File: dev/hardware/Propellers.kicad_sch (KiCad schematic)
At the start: 6 parts, among them SW1 RESET SW, U1 P8X32A-D40, Y1 6.5MHz

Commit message: Continued developing JCAP schematic
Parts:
- added C1, C2: 0.1u, Capacitor_THT:C_Radial_D4.0mm_H7.0mm_P1.50mm, symbol Device:C
- added R1: 1K, Resistor_THT:R_Axial_DIN0207_L6.3mm_D2.5mm_P10.16mm_Horizontal, symbol Device:R
- added SW1: RESET SW, symbol Switch:SW_MEC_5E
- added U1: P8X32A-D40, Package_DIP:DIP-40_W15.24mm_Socket, symbol MCU_Parallax:P8X32A-D40
- added Y1: 6.5MHz, Crystal:Crystal_HC49-U_Vertical, symbol Device:Crystal
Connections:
- net +3.3V: now also C1.2, C2.1
- net GND: now also R1.1, U1.10 (~{BOE}), U1.29 (VSS), U1.9 (VSS)
- net INPUTS_CLK: now reaches U1.34 (P25)
- net INPUTS_PL_N: now reaches U1.35 (P26)
- net INPUTS: now reaches U1.36 (P27)
- net SCL_CPU: now reaches U1.37 (P28)
- net SDA_CPU: now reaches U1.38 (P29)
- net SER_TX_CPU: now reaches U1.39 (P30)
- net SER_RX_CPU: now reaches U1.40 (P31)
- net SER_RES_N_CPU: now reaches SW1.3 (K)
- new net: C1.1, U1.12 (VDD)
- new net: U1.31 (XO), Y1.1
- new net: U1.30 (XI), Y1.2
- new net: SW1.4 (A), U1.11 (~{RES})
- new net: C2.2, U1.32 (VDD)
- new net: R1.2, SW1.1
- new net BLUE0: U1.27 (P22)
- new net BLUE1: U1.28 (P23)
- new net GREEN0: U1.24 (P19)
- new net GREEN1: U1.25 (P20)
- new net GREEN2: U1.26 (P21)
- new net H_SYNC: U1.34 (P25)
- new net RED0: U1.21 (P16)
- new net RED1: U1.22 (P17)
- new net RED2: U1.23 (P18)
- new net SCL_GPU: U1.37 (P28)
- new net SDA_GPU: U1.38 (P29)
- new net SER_RES_N_GPU: SW1.3 (K)
- new net SER_RX_GPU: U1.40 (P31)
- new net SER_TX_GPU: U1.39 (P30)
- new net V_SYNC: U1.33 (P24)
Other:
- moved on the sheet: C1, C2, R1, SW1, U1, Y1

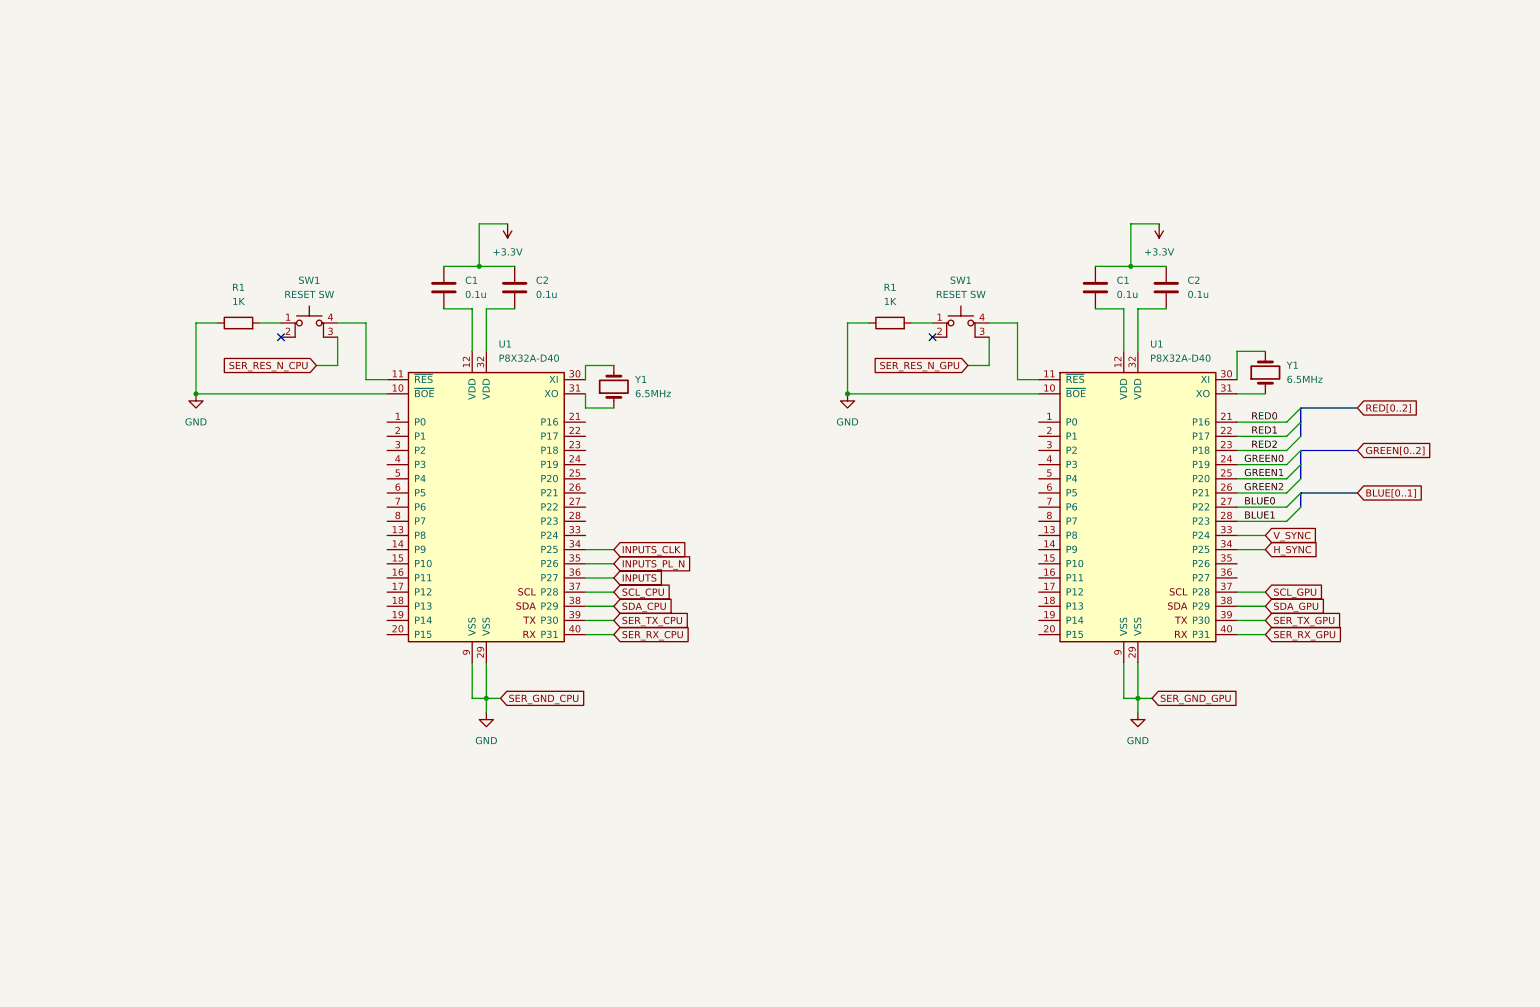
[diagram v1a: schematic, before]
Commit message: Finalized initial schematic
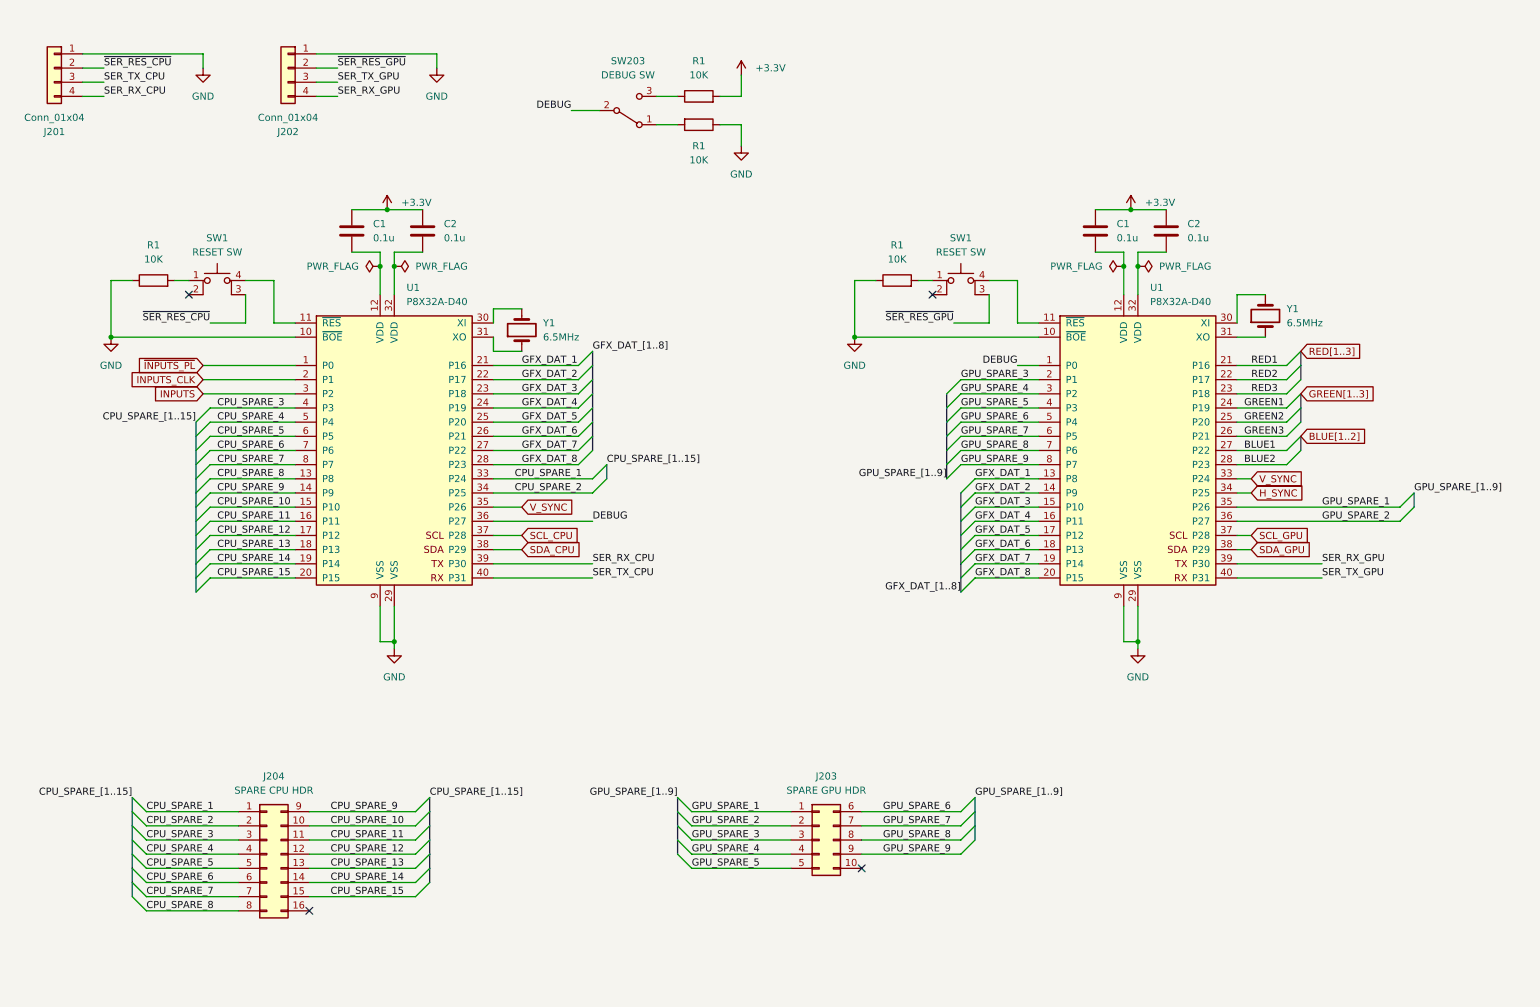
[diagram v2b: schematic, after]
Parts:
- removed R1 (x2): 1K, Resistor_THT:R_Axial_DIN0207_L6.3mm_D2.5mm_P10.16mm_Horizontal, symbol Device:R
- removed SW1 (x2): RESET SW, symbol Switch:SW_MEC_5E
- added J201, J202: Conn_01x04, Connector_PinHeader_2.54mm:PinHeader_1x04_P2.54mm_Horizontal, symbol Connector_Generic:Conn_01x04
- added J203: SPARE GPU HDR, Connector_PinHeader_2.54mm:PinHeader_2x05_P2.54mm_Vertical, symbol Connector_Generic:Conn_02x05_Top_Bottom
- added J204: SPARE CPU HDR, Connector_PinHeader_2.54mm:PinHeader_2x08_P2.54mm_Vertical, symbol Connector_Generic:Conn_02x08_Top_Bottom
- added R1 (x4): 10K, Resistor_THT:R_Axial_DIN0207_L6.3mm_D2.5mm_P10.16mm_Horizontal, symbol Device:R
- added SW1 (x2): RESET SW, Button_Switch_THT:SW_PUSH_6mm_H5mm, symbol Switch:SW_MEC_5E
- added SW203: DEBUG SW, Button_Switch_THT:SW_E-Switch_EG1271_SPDT, symbol Switch:SW_SPDT
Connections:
- net BLUE0 is gone; now on net BLUE1: U1.27 (P22)
- net GREEN0 is gone; now on net GREEN1: U1.24 (P19)
- net INPUTS_PL_N is gone; now on net V_SYNC: U1.35 (P26)
- net RED0 is gone; now on net RED1: U1.21 (P16)
- net +3.3V: now also R1.2
- net BLUE1: no longer U1.28 (P23)
- net GND: now also J201.1 (Pin_1), J202.1 (Pin_1), R1.1, R1.1, R1.1
- net GREEN1: no longer U1.25 (P20)
- net GREEN2: now also U1.25 (P20); no longer U1.26 (P21)
- net INPUTS: now also U1.3 (P2); no longer U1.36 (P27)
- net INPUTS_CLK: now also U1.2 (P1); no longer U1.34 (P25)
- net RED1: no longer U1.22 (P17)
- net RED2: now also U1.22 (P17); no longer U1.23 (P18)
- net SER_RX_CPU: now also U1.39 (P30), J201.4 (Pin_4); no longer U1.40 (P31)
- net SER_RX_GPU: now also U1.39 (P30), J202.4 (Pin_4); no longer U1.40 (P31)
- net SER_TX_CPU: now also U1.40 (P31), J201.3 (Pin_3); no longer U1.39 (P30)
- net SER_TX_GPU: now also U1.40 (P31), J202.3 (Pin_3); no longer U1.39 (P30)
- net DEBUG: now reaches U1.1 (P0)
- net DEBUG: now also U1.36 (P27), SW203.2 (B)
- net at U1.11 (~{RES}): now also SW1.4 (A) (x2)
- net GFX_DAT_1: now reaches U1.13 (P8)
- net GFX_DAT_1: now also U1.21 (P16)
- net GFX_DAT_2: now reaches U1.14 (P9)
- net GFX_DAT_2: now also U1.22 (P17)
- net GFX_DAT_3: now reaches U1.15 (P10)
- net GFX_DAT_3: now also U1.23 (P18)
- net GFX_DAT_4: now reaches U1.16 (P11)
- net GFX_DAT_4: now also U1.24 (P19)
- net GFX_DAT_5: now reaches U1.17 (P12)
- net GFX_DAT_5: now also U1.25 (P20)
- net GFX_DAT_6: now reaches U1.18 (P13)
- net GFX_DAT_6: now also U1.26 (P21)
- net GFX_DAT_7: now reaches U1.19 (P14)
- net GFX_DAT_7: now also U1.27 (P22)
- net GPU_SPARE_3: now reaches U1.2 (P1)
- net GPU_SPARE_3: now also J203.3 (Pin_3)
- net GFX_DAT_8: now reaches U1.20 (P15)
- net GFX_DAT_8: now also U1.28 (P23)
- net GPU_SPARE_4: now reaches U1.3 (P2)
- net GPU_SPARE_4: now also J203.4 (Pin_4)
- net GPU_SPARE_1: now reaches U1.35 (P26)
- net GPU_SPARE_1: now also J203.1 (Pin_1)
- net GPU_SPARE_2: now reaches U1.36 (P27)
- net GPU_SPARE_2: now also J203.2 (Pin_2)
- net GPU_SPARE_5: now reaches U1.4 (P3)
- net GPU_SPARE_5: now also J203.5 (Pin_5)
- net GPU_SPARE_6: now reaches U1.5 (P4)
- net GPU_SPARE_6: now also J203.6 (Pin_6)
- net GPU_SPARE_7: now reaches U1.6 (P5)
- net GPU_SPARE_7: now also J203.7 (Pin_7)
- net GPU_SPARE_8: now reaches U1.7 (P6)
- net GPU_SPARE_8: now also J203.8 (Pin_8)
- net GPU_SPARE_9: now reaches U1.8 (P7)
- net GPU_SPARE_9: now also J203.9 (Pin_9)
- net ~{INPUTS_PL}: now reaches U1.1 (P0)
- net CPU_SPARE_8: now reaches U1.13 (P8)
- net CPU_SPARE_8: now also J204.8 (Pin_8)
- net CPU_SPARE_9: now reaches U1.14 (P9)
- net CPU_SPARE_9: now also J204.9 (Pin_9)
- net CPU_SPARE_10: now reaches U1.15 (P10)
- net CPU_SPARE_10: now also J204.10 (Pin_10)
- net CPU_SPARE_11: now reaches U1.16 (P11)
- net CPU_SPARE_11: now also J204.11 (Pin_11)
- net CPU_SPARE_12: now reaches U1.17 (P12)
- net CPU_SPARE_12: now also J204.12 (Pin_12)
- net CPU_SPARE_13: now reaches U1.18 (P13)
- net CPU_SPARE_13: now also J204.13 (Pin_13)
- net CPU_SPARE_14: now reaches U1.19 (P14)
- net CPU_SPARE_14: now also J204.14 (Pin_14)
- net CPU_SPARE_15: now reaches U1.20 (P15)
- net CPU_SPARE_15: now also J204.15 (Pin_15)
- net CPU_SPARE_1: now reaches U1.33 (P24)
- net CPU_SPARE_1: now also J204.1 (Pin_1)
- net CPU_SPARE_3: now reaches U1.4 (P3)
- net CPU_SPARE_3: now also J204.3 (Pin_3)
- net CPU_SPARE_4: now reaches U1.5 (P4)
- net CPU_SPARE_4: now also J204.4 (Pin_4)
- net CPU_SPARE_5: now reaches U1.6 (P5)
- net CPU_SPARE_5: now also J204.5 (Pin_5)
- net CPU_SPARE_6: now reaches U1.7 (P6)
- net CPU_SPARE_6: now also J204.6 (Pin_6)
- net CPU_SPARE_7: now reaches U1.8 (P7)
- net CPU_SPARE_7: now also J204.7 (Pin_7)
- new net: R1.2, SW203.1 (A)
- new net: R1.1, SW203.3 (C)
- new net: R1.2, SW1.1 (x2)
- new net BLUE2: U1.28 (P23)
- new net CPU_SPARE_2: J204.2 (Pin_2), U1.34 (P25)
- new net GREEN3: U1.26 (P21)
- new net RED3: U1.23 (P18)
- new net ~{SER_RES_CPU}: J201.2 (Pin_2), SW1.3 (K)
- new net ~{SER_RES_GPU}: J202.2 (Pin_2), SW1.3 (K)
- no-connect marks 2 -> 4
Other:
- moved on the sheet: C1, C2, U1, Y1

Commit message: Started developing PCB layout
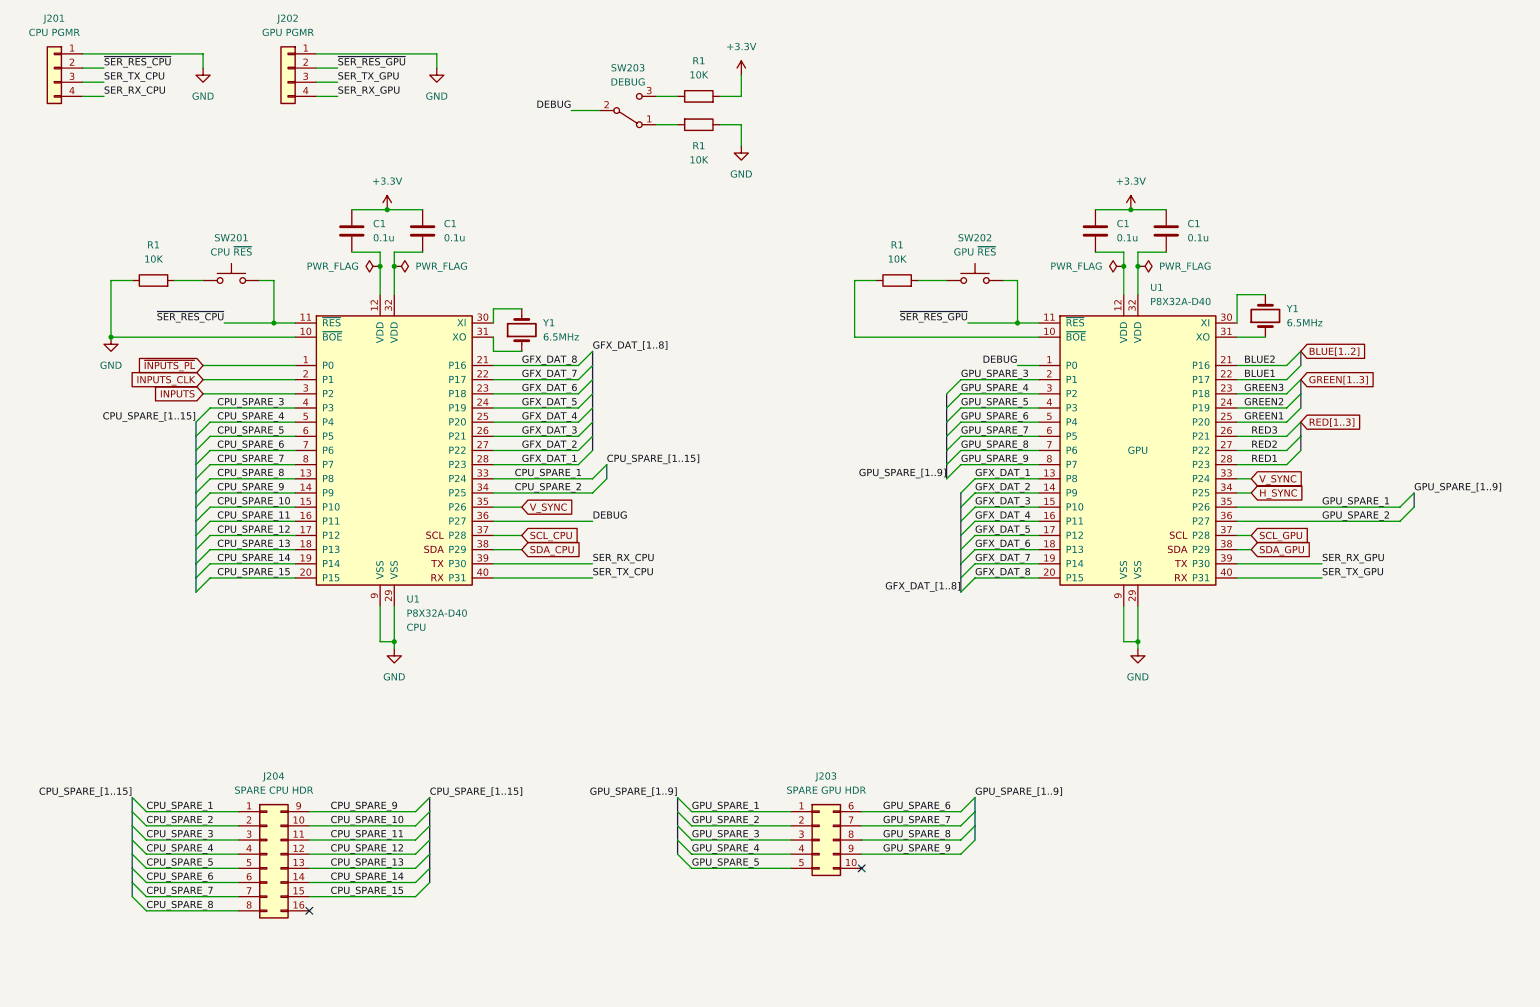
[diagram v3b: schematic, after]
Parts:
- removed C1, C2 (x2): 0.1u, Capacitor_THT:C_Radial_D4.0mm_H7.0mm_P1.50mm, symbol Device:C
- removed SW1 (x2): RESET SW, Button_Switch_THT:SW_PUSH_6mm_H5mm, symbol Switch:SW_MEC_5E
- added C1 (x3): 0.1u, Capacitor_THT:C_Disc_D3.4mm_W2.1mm_P2.50mm, symbol Device:C
- added SW201: CPU ~{RES}, Button_Switch_THT:SW_PUSH_6mm_H5mm, symbol Switch:SW_Push
- added SW202: GPU ~{RES}, Button_Switch_THT:SW_PUSH_6mm_H5mm, symbol Switch:SW_Push
- C1: footprint Capacitor_THT:C_Radial_D4.0mm_H7.0mm_P1.50mm -> Capacitor_THT:C_Disc_D3.4mm_W2.1mm_P2.50mm
- J201: value Conn_01x04 -> CPU PGMR
- J202: value Conn_01x04 -> GPU PGMR
- SW203: value DEBUG SW -> DEBUG; footprint Button_Switch_THT:SW_E-Switch_EG1271_SPDT -> Button_Switch_THT:SW_Slide_1P2T_CK_OS102011MS2Q
- U1: Role (none) -> GPU
- U1: Role (none) -> CPU
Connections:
- net +3.3V: now also C1.2, C1.2, C1.2
- net BLUE1: now also U1.22 (P17); no longer U1.27 (P22)
- net BLUE2: now also U1.21 (P16); no longer U1.28 (P23)
- net GFX_DAT_1: now also U1.28 (P23); no longer U1.21 (P16)
- net GFX_DAT_2: now also U1.27 (P22); no longer U1.22 (P17)
- net GFX_DAT_3: now also U1.26 (P21); no longer U1.23 (P18)
- net GFX_DAT_4: now also U1.25 (P20); no longer U1.24 (P19)
- net GFX_DAT_5: now also U1.24 (P19); no longer U1.25 (P20)
- net GFX_DAT_6: now also U1.23 (P18); no longer U1.26 (P21)
- net GFX_DAT_7: now also U1.22 (P17); no longer U1.27 (P22)
- net GFX_DAT_8: now also U1.21 (P16); no longer U1.28 (P23)
- net GND: no longer R1.1, U1.10 (~{BOE})
- net GREEN1: now also U1.25 (P20); no longer U1.24 (P19)
- net GREEN2: now also U1.24 (P19); no longer U1.25 (P20)
- net GREEN3: now also U1.23 (P18); no longer U1.26 (P21)
- net RED1: now also U1.28 (P23); no longer U1.21 (P16)
- net RED2: now also U1.27 (P22); no longer U1.22 (P17)
- net RED3: now also U1.26 (P21); no longer U1.23 (P18)
- net ~{SER_RES_CPU}: now also U1.11 (~{RES}), SW201.2
- net ~{SER_RES_GPU}: now also U1.11 (~{RES}), SW202.2
- net at R1.2: now also SW201.1
- net at R1.2: now also SW202.1
- net at U1.12 (VDD): now also C1.1
- net at U1.32 (VDD): now also C1.1 (x2)
- new net: R1.1, U1.10 (~{BOE})
- no-connect marks 4 -> 2

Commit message: Fixed resistors and reset PCB
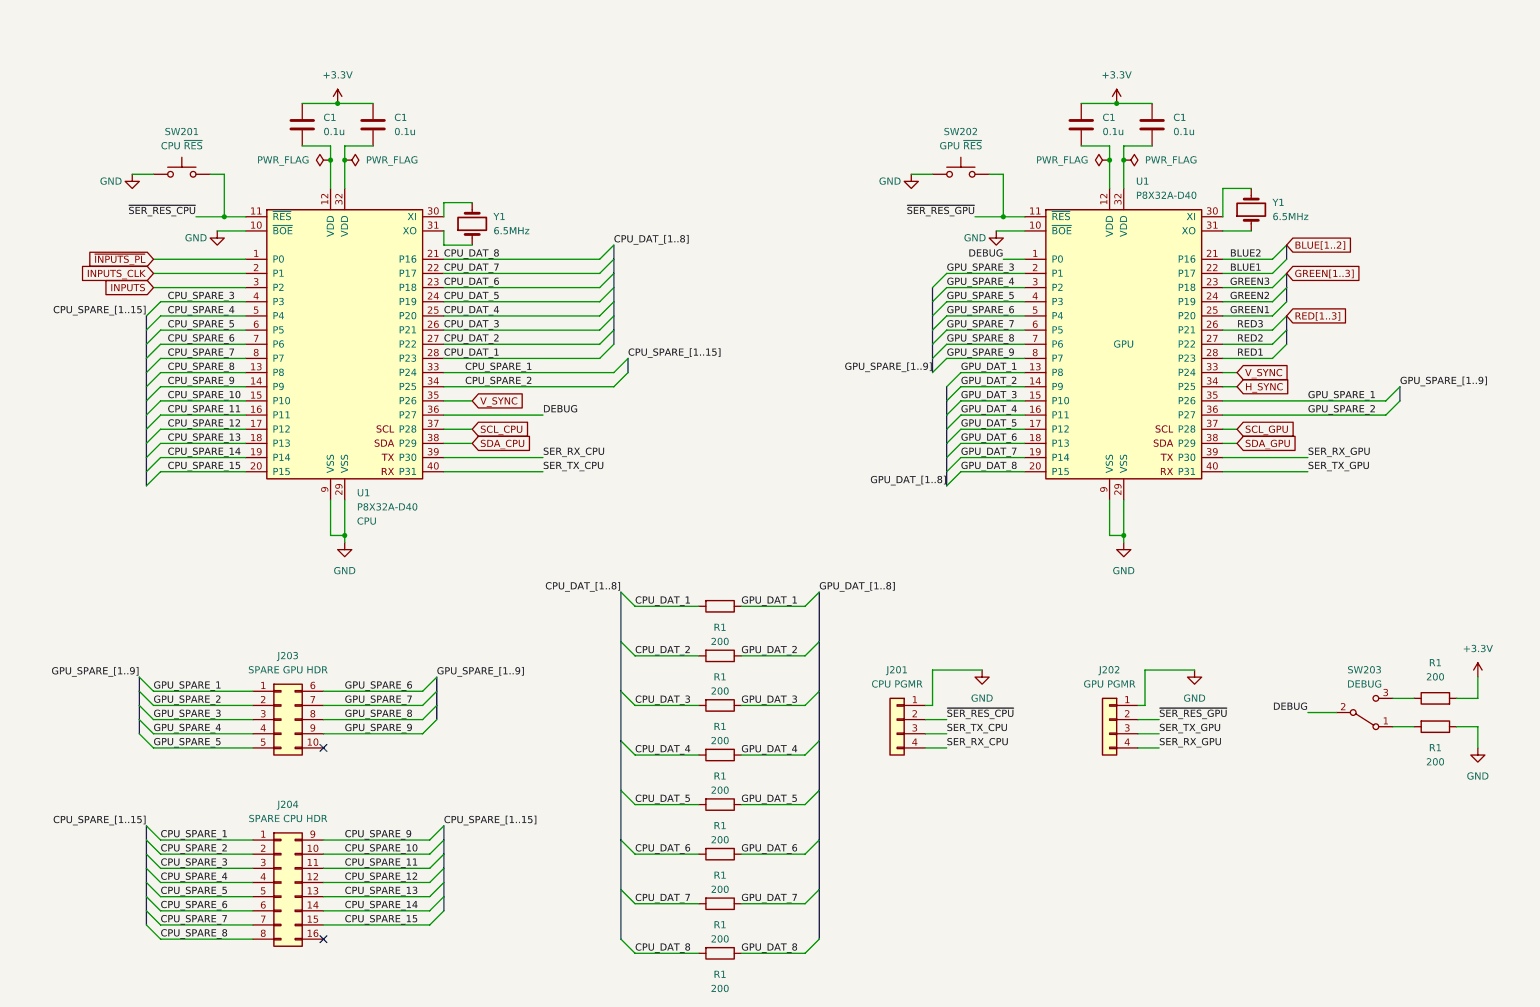
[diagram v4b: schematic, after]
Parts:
- removed R1 (x2): 10K, Resistor_THT:R_Axial_DIN0207_L6.3mm_D2.5mm_P10.16mm_Horizontal, symbol Device:R
- added R1 (x8): 200, Resistor_THT:R_Axial_DIN0207_L6.3mm_D2.5mm_P10.16mm_Horizontal, symbol Device:R
- R1: value 10K -> 200
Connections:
- net GND: now also SW201.1, SW202.1, U1.10 (~{BOE})
- net GFX_DAT_1 renamed CPU_DAT_1
- net CPU_DAT_1: now also R1.2; no longer U1.13 (P8)
- net GFX_DAT_2 renamed CPU_DAT_2
- net CPU_DAT_2: now also R1.2; no longer U1.14 (P9)
- net GFX_DAT_3 renamed CPU_DAT_3
- net CPU_DAT_3: now also R1.2; no longer U1.15 (P10)
- net GFX_DAT_4 renamed CPU_DAT_4
- net CPU_DAT_4: now also R1.2; no longer U1.16 (P11)
- net GFX_DAT_5 renamed CPU_DAT_5
- net CPU_DAT_5: now also R1.2; no longer U1.17 (P12)
- net GFX_DAT_6 renamed CPU_DAT_6
- net CPU_DAT_6: now also R1.2; no longer U1.18 (P13)
- net GFX_DAT_7 renamed CPU_DAT_7
- net CPU_DAT_7: now also R1.2; no longer U1.19 (P14)
- net GFX_DAT_8 renamed CPU_DAT_8
- net CPU_DAT_8: now also R1.2; no longer U1.20 (P15)
- new net GPU_DAT_1: R1.1, U1.13 (P8)
- new net GPU_DAT_2: R1.1, U1.14 (P9)
- new net GPU_DAT_3: R1.1, U1.15 (P10)
- new net GPU_DAT_4: R1.1, U1.16 (P11)
- new net GPU_DAT_5: R1.1, U1.17 (P12)
- new net GPU_DAT_6: R1.1, U1.18 (P13)
- new net GPU_DAT_7: R1.1, U1.19 (P14)
- new net GPU_DAT_8: R1.1, U1.20 (P15)
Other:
- moved on the sheet: C1, J201, J202, J203, J204, R1, SW201, SW203, U1, Y1
